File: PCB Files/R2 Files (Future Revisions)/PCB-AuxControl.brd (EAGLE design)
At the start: 77.5 x 63.2 mm, 16 parts, among them K1 JZC-11F, K2 JZC-11F, T1 NPN2222A, T2 NPN2222A

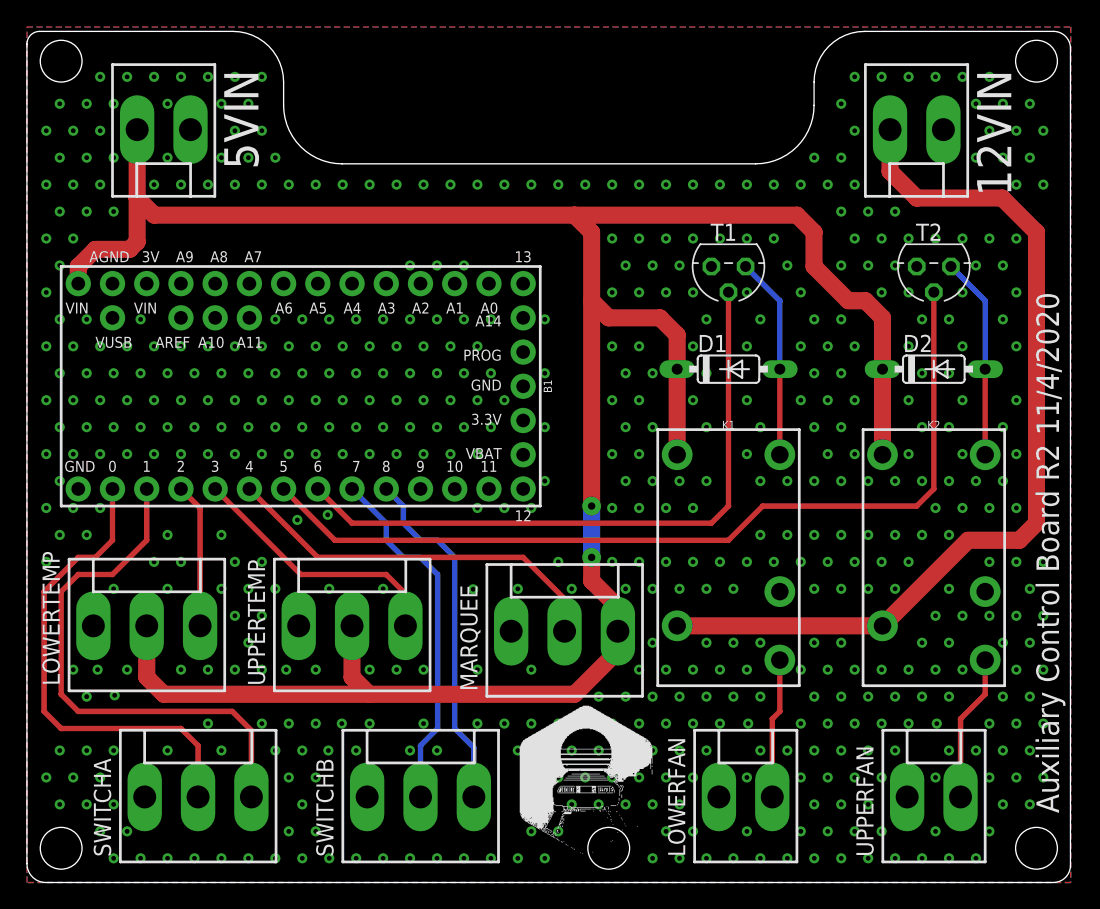
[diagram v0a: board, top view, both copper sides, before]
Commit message: AUX Control PCB Update
Added a 4 pin header to the Aux Control PCB to add a remote 2x20 IC Screen for Status/ Cabinet Temp display.
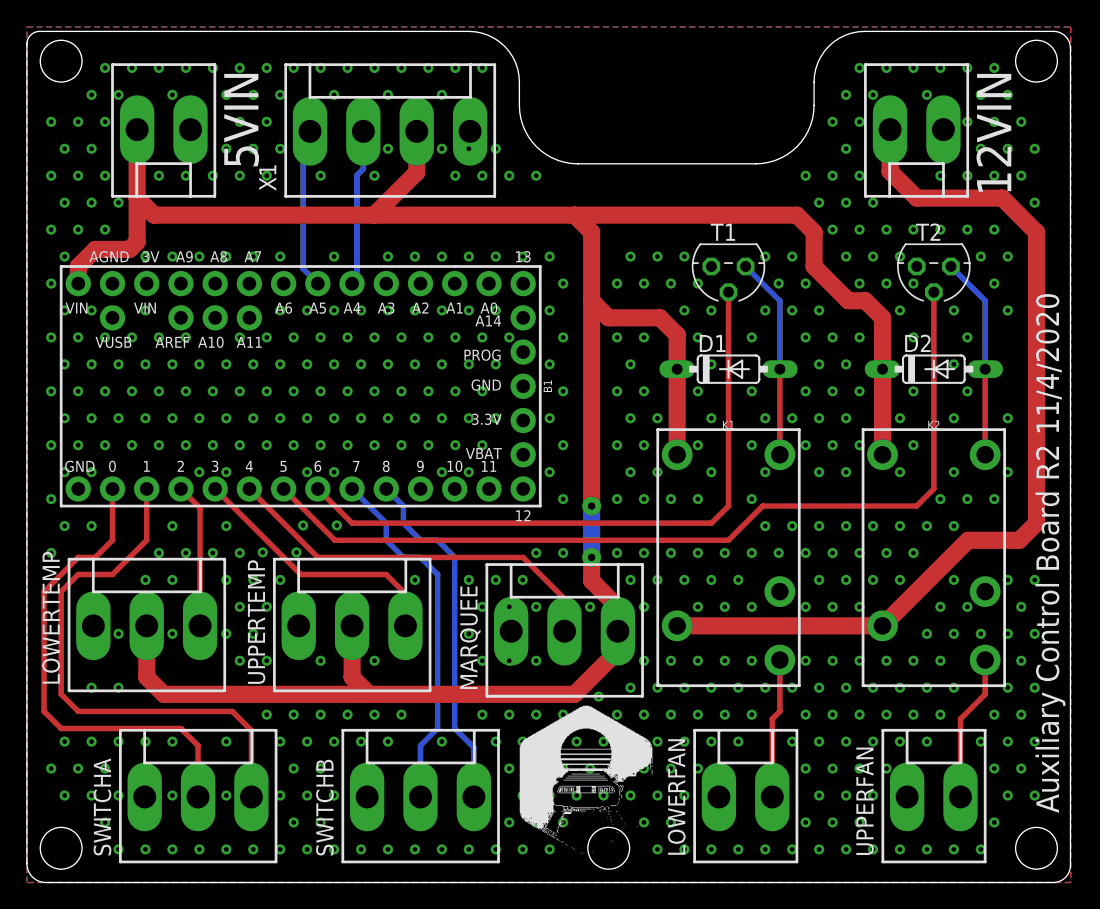
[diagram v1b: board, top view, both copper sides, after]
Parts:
- added X1: (no value), con-molex:KK-156-4
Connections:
- new net CLK: B1.19, X1.1
- new net DAT: B1.18, X1.2
- net 5VIN: now also X1.3
- net GND: now also X1.4
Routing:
- net CLK: track 0.00 -> 12.0 mm
- net DAT: track 0.00 -> 11.6 mm
- net 5VIN: track 181.6 -> 189.1 mm
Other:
- outline, holes or cut-outs redrawn
- board text added: "11-4-2020 - (R2) - CHANGED MARQUEE MOLEX FROM 2 PIN TO 3 PIN TO ADD 5V TO HEADER. 5VIN WAS CHANGED FROM .8068 THICKNESS TO 1.27 FOR ADDITIONAL POWER NEEDS 12-9-2020 - (R2a) - ADDED HEADER FOR I2C 2X20 SCREEN"
- board text removed: "11-4-2020 - (R2) - CHANGED MARQUEE MOLEX FROM 2 PIN TO 3 PIN TO ADD 5V TO HEADER. 5VIN WAS CHANGED FROM .8068 THICKNESS TO 1.27 FOR ADDITIONAL POWER NEEDS"
